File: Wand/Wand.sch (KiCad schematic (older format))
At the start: 27 parts, among them P1 ISP, P2 KLB4, P3 BASE, U1 ATMEGA328-MMH, U2 OPA336, U3 MPU-6050

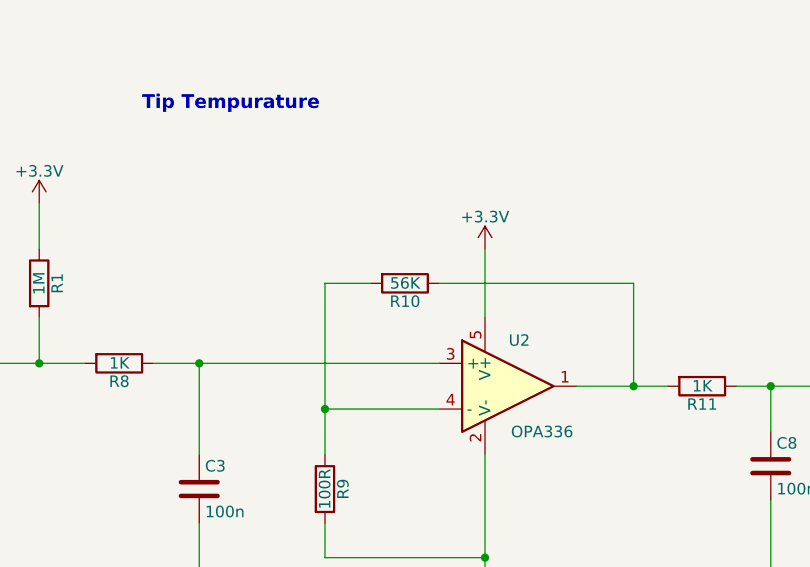
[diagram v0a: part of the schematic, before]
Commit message: Updated resister values with those from the prototype
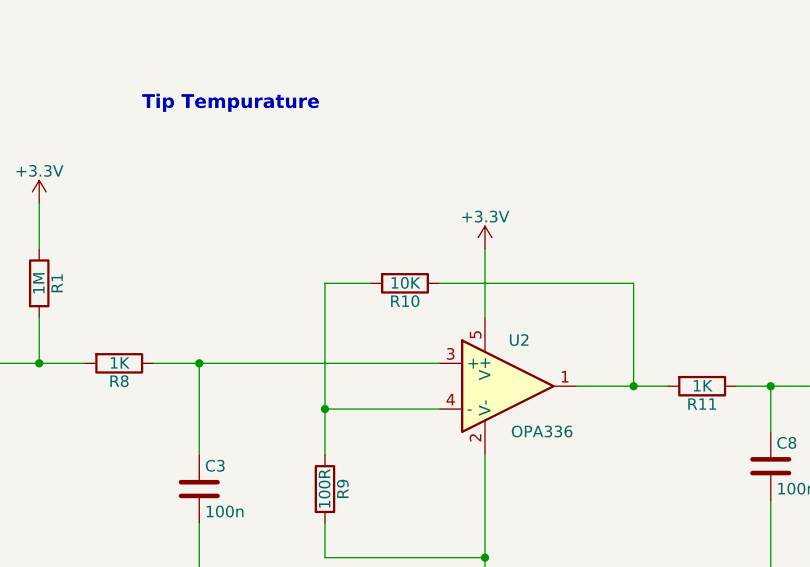
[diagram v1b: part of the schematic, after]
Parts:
- R10: value 56K -> 10K
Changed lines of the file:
@@
 P 2800 5500
 F 0 "R10" V 2880 5500 50  0000 C CNN
-F 1 "56K" V 2800 5500 50  0000 C CNN
+F 1 "10K" V 2800 5500 50  0000 C CNN
 F 2 "Resistors_SMD:R_0402" V 2730 5500 50  0001 C CNN
 F 3 "" H 2800 5500 50  0000 C CNN
